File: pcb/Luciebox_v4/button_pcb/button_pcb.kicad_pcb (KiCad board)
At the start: 2 copper layers, 144 x 157.6 mm, 67 parts, among them T1 terminal_8x1, T2 terminal_8x1

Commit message: V4 main pcb ready for layouting
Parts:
- removed D1, D2, D3, D4, D5, D6, D7, D8: D_Schottky, Luciebox:smd_throughhole_2_pins
- removed the H1 at (110.8, 86.4)
- removed H10, H12, H14, H15, H17, H9: MountingHole, Luciebox:MountingHole_4.3mm_M4
- removed the H7 at (17.5, -38.4)
- removed the H8 at (77.5, -38.4)
- removed R1: R_Small, Luciebox:SIP-10
- removed R10, R11, R12, R13, R14, R15, R16, R17, R18, R2, R3, R4, R5, R6, R7, R8, R9: R_Small, Luciebox:1206_0805
- removed R19, R20, R21, R22, R23, R24, R25, R26, R27, R28, R29, R30: 10K, Luciebox_components:1206_0805
- removed S9: selector_knob, Luciebox_components:Rotary_Switch
- added BT1: 4xAA_Battery_holder, Luciebox_components:BatteryHolder_4xAA, B.Cu at (70.3, 89.1)
- added T3: terminal_8x1, Luciebox_components:Terminal_8x1_100mil, F.Cu at (19.1, 33.0)
- added T4: terminal_2x1, Luciebox_components:Terminal_2x1_100mil, F.Cu at (72.0, 28.5)
- H1: renamed from H16; footprint Luciebox:MountingHole_4.3mm_M4 -> Luciebox_components:MountingHole_4.3mm_M4
- H2: renamed from H6; footprint Luciebox:MountingHole_4.3mm_M4 -> Luciebox_components:MountingHole_4.3mm_M4
- H3: renamed from H13; footprint Luciebox:MountingHole_4.3mm_M4 -> Luciebox_components:MountingHole_4.3mm_M4
- H4: renamed from H11; footprint Luciebox:MountingHole_4.3mm_M4 -> Luciebox_components:MountingHole_4.3mm_M4
- H5: footprint Luciebox:MountingHole_4.3mm_M4 -> Luciebox_components:MountingHole_4.3mm_M4
- H6: renamed from H3; footprint Luciebox:MountingHole_4.3mm_M4 -> Luciebox_components:MountingHole_4.3mm_M4
- H7: renamed from H2; footprint Luciebox:MountingHole_4.3mm_M4 -> Luciebox_components:MountingHole_4.3mm_M4
- H8: renamed from H4; footprint Luciebox:MountingHole_4.3mm_M4 -> Luciebox_components:MountingHole_4.3mm_M4
- S1, S2, S3, S4, S5, S6, S7, S8: footprint Luciebox:button_LAZ16-11 -> Luciebox_components:button_LAZ16-11_big_holes
- T1, T2: footprint Luciebox:Terminal_8x1_100mil -> Luciebox_components:Terminal_8x1_100mil
- connect_for_vcc_as_common_anode1: footprint Luciebox:1206_0805 -> Luciebox_components:1206_0805
- moved H3 113.5 mm to (72.0, 61.0)
- moved H6 90.3 mm to (58.0, 25.0)
- moved connect_for_vcc_as_common_anode1 87.3 mm to (74.5, 34.0), turned to 90 degrees
- moved H7 76.1 mm to (58.0, 86.5)
- moved H8 66.2 mm to (20.0, 86.5)
- moved H5 52.9 mm to (20.0, 25.0)
- moved H2 47.7 mm to (72.0, 6.00)
- moved H1 40.5 mm to (6.00, 6.00)
- moved H4 38.5 mm to (6.00, 61.0)
- moved T2 27.4 mm to (39.4, 33.0)
- moved T1 7.48 mm to (59.7, 33.0)
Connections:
- S1 pad 5: VCC -> Net-(S1-Pad5)
- S2 pad 5: VCC -> Net-(S2-Pad5)
- S3 pad 5: VCC -> Net-(S3-Pad5)
- S4 pad 5: Net-(D4-Pad2) -> Net-(T2-Pad4)
- S5 pad 5: Net-(D5-Pad2) -> Net-(S5-Pad5)
- S6 pad 5: Net-(D6-Pad2) -> Net-(T2-Pad6)
- S7 pad 5: Net-(D7-Pad2) -> Net-(T2-Pad7)
- S8 pad 5: Net-(D8-Pad2) -> Net-(S8-Pad5)
- T1 pad 3: /ANALOG_1 -> Net-(S1-Pad4)
- T1 pad 4: /ANALOG_2 -> Net-(T1-Pad4)
- T1 pad 6: Net-(S1-Pad4) -> unconnected-(T1-Pad6)
- T2 pad 1: Net-(D1-Pad1) -> Net-(S1-Pad5)
- T2 pad 2: Net-(D2-Pad1) -> Net-(S2-Pad5)
- T2 pad 3: Net-(D3-Pad1) -> Net-(S3-Pad5)
- T2 pad 4: Net-(D4-Pad1) -> Net-(T2-Pad4)
- T2 pad 5: Net-(D5-Pad1) -> Net-(S5-Pad5)
- T2 pad 6: Net-(D6-Pad1) -> Net-(T2-Pad6)
- T2 pad 7: Net-(D7-Pad1) -> Net-(T2-Pad7)
- T2 pad 8: Net-(D8-Pad1) -> Net-(S8-Pad5)
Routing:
- net VCC: track 0.00 -> 244.7 mm, vias 0 -> 9
- net GND: track 0.00 -> 197.4 mm, vias 0 -> 1
- net Net-(S1-Pad4): track 0.00 -> 191.4 mm
- net Net-(S3-Pad3): track 0.00 -> 146.4 mm
- net Net-(S1-Pad5): track 0.00 -> 131.8 mm
- net Net-(T2-Pad4): track 0.00 -> 126.6 mm
- net Net-(S4-Pad3): track 0.00 -> 119.2 mm, vias 0 -> 5
- net Net-(S3-Pad5): track 0.00 -> 116.4 mm
- net Net-(S2-Pad5): track 0.00 -> 115.1 mm
- net Net-(S8-Pad3): track 0.00 -> 76.2 mm
- net Net-(S2-Pad3): track 0.00 -> 68.9 mm
- net Net-(S1-Pad3): track 0.00 -> 53.3 mm
- net Net-(S8-Pad5): track 0.00 -> 47.5 mm
- net Net-(S5-Pad5): track 0.00 -> 47.0 mm
- net Net-(S7-Pad3): track 0.00 -> 39.0 mm
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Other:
- board size 144 x 157.6 mm -> 78 x 100 mm
- board text added: "BAT+"
- board text added: "BAT-"
- board text added: "buttonsboard v2.0 2022-05 a luciebox extension by nonkel lode putting extra pret in the bak kicad project: button_pcb_4x_laz16-11"
- board text removed: "M2 M2.5 M3 M4"
- board text removed: "M5"
- board text removed: "M6"
- board text removed: "M8"
- board text removed: "buttonsboard v1.1 2020-12 a luciebox extension by nonkel lode putting extra pret in the bak kicad project: button_pcb_4x_laz16-11"

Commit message: layout main board start
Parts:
- added U1: 8X8PADS, Luciebox_components:8X8PADS_100mil, F.Cu at (40.2, 15.0)
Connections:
- net Net-(S1-Pad4) renamed /common Anode
- S1 pad 1: VCC -> Net-(BT1-Pad1)
- S1 pad 2: GND -> Net-(S1-Pad2)
- T1 pad 5: Net-(T1-Pad5) -> Net-(BT1-Pad1)
- T1 pad 6: unconnected-(T1-Pad6) -> Net-(S1-Pad2)
- T1 pad 7: unconnected-(T1-Pad7) -> Net-(S1-Pad3)
- T3 pad 1: Net-(S1-Pad3) -> unconnected-(T3-Pad1)
- T4 pad 2: Net-(T1-Pad5) -> Net-(BT1-Pad1)
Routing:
- net Net-(T1-Pad5): track 12.9 -> 0.00 mm
- net Net-(BT1-Pad1): track 0.00 -> 12.9 mm

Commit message: Delete Arduino Uno footprint. Line up bottonboard and main pcb
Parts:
- moved H5 14.0 mm to (6.00, 25.4)
- moved H6 14.0 mm to (72.0, 25.4)
- moved T4 5.99 mm to (66.0, 27.9)
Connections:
- U1 pad 1: unconnected-(U1-Pad1) -> VCC
- U1 pad 10: unconnected-(U1-Pad10) -> Net-(U1-Pad10)
- U1 pad 11: unconnected-(U1-Pad11) -> Net-(U1-Pad11)
- U1 pad 12: unconnected-(U1-Pad12) -> Net-(U1-Pad11)
- U1 pad 13: unconnected-(U1-Pad13) -> Net-(U1-Pad14)
- U1 pad 14: unconnected-(U1-Pad14) -> Net-(U1-Pad14)
- U1 pad 15: unconnected-(U1-Pad15) -> Net-(U1-Pad14)
- U1 pad 16: unconnected-(U1-Pad16) -> Net-(U1-Pad14)
- U1 pad 17: unconnected-(U1-Pad17) -> Net-(U1-Pad17)
- U1 pad 18: unconnected-(U1-Pad18) -> Net-(U1-Pad17)
- U1 pad 19: unconnected-(U1-Pad19) -> Net-(U1-Pad19)
- U1 pad 2: unconnected-(U1-Pad2) -> VCC
- U1 pad 20: unconnected-(U1-Pad20) -> Net-(U1-Pad19)
- U1 pad 21: unconnected-(U1-Pad21) -> Net-(U1-Pad21)
- U1 pad 22: unconnected-(U1-Pad22) -> Net-(U1-Pad21)
- U1 pad 23: unconnected-(U1-Pad23) -> Net-(U1-Pad21)
- U1 pad 24: unconnected-(U1-Pad24) -> Net-(U1-Pad21)
- U1 pad 3: unconnected-(U1-Pad3) -> VCC
- U1 pad 30: unconnected-(U1-Pad30) -> Net-(U1-Pad30)
- U1 pad 31: unconnected-(U1-Pad31) -> Net-(U1-Pad30)
- U1 pad 32: unconnected-(U1-Pad32) -> Net-(U1-Pad30)
- U1 pad 38: unconnected-(U1-Pad38) -> Net-(U1-Pad38)
- U1 pad 39: unconnected-(U1-Pad39) -> Net-(U1-Pad38)
- U1 pad 4: unconnected-(U1-Pad4) -> VCC
- U1 pad 40: unconnected-(U1-Pad40) -> Net-(U1-Pad38)
- U1 pad 46: unconnected-(U1-Pad46) -> Net-(U1-Pad46)
- U1 pad 47: unconnected-(U1-Pad47) -> Net-(U1-Pad46)
- U1 pad 48: unconnected-(U1-Pad48) -> Net-(U1-Pad46)
- U1 pad 5: unconnected-(U1-Pad5) -> VCC
- U1 pad 54: unconnected-(U1-Pad54) -> Net-(U1-Pad54)
- U1 pad 55: unconnected-(U1-Pad55) -> Net-(U1-Pad54)
- U1 pad 56: unconnected-(U1-Pad56) -> Net-(U1-Pad54)
- U1 pad 57: unconnected-(U1-Pad57) -> GND
- U1 pad 58: unconnected-(U1-Pad58) -> GND
- U1 pad 59: unconnected-(U1-Pad59) -> GND
- U1 pad 6: unconnected-(U1-Pad6) -> VCC
- U1 pad 60: unconnected-(U1-Pad60) -> GND
- U1 pad 61: unconnected-(U1-Pad61) -> GND
- U1 pad 62: unconnected-(U1-Pad62) -> GND
- U1 pad 63: unconnected-(U1-Pad63) -> GND
- U1 pad 64: unconnected-(U1-Pad64) -> GND
- U1 pad 7: unconnected-(U1-Pad7) -> VCC
- U1 pad 8: unconnected-(U1-Pad8) -> VCC
- U1 pad 9: unconnected-(U1-Pad9) -> Net-(U1-Pad10)
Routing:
- net unconnected-(T3-Pad1): track 0.00 -> 53.3 mm
- net Net-(S1-Pad3): track 53.3 -> 0.00 mm
- net Net-(BT1-Pad1): track 12.9 -> 7.18 mm
- net Net-(BT1-Pad2): track 12.9 -> 7.18 mm

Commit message: Main board pcb prevent interference with buttons from button board
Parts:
- moved T4 4.07 mm to (65.0, 24.0)
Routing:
- net Net-(BT1-Pad2): track 7.18 -> 10.7 mm
- net Net-(BT1-Pad1): track 7.18 -> 10.7 mm
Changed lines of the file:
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@@
       (net 17 "Net-(S7-Pad5)") (pinfunction "LED_-") (pintype "input"))
   )
-  (footprint "Luciebox_components:Terminal_8x1_100mil" locked (layer "F.Cu")
+  (footprint "Luciebox_components:Terminal_8x1_100mil" (layer "F.Cu")
     (at 39.37 33.02)
     (property "Sheetfile" "button_pcb.kicad_sch")
@@
       (clearance 2))
   )
-  (footprint "Luciebox_components:Terminal_8x1_100mil" locked (layer "F.Cu")
+  (footprint "Luciebox_components:Terminal_8x1_100mil" (layer "F.Cu")
     (at 59.69 33.02)
     (property "Sheetfile" "button_pcb.kicad_sch")
@@
       (net 16 "Net-(S6-Pad5)") (pinfunction "LED_-") (pintype "input"))
   )
-  (footprint "Luciebox_components:Terminal_8x1_100mil" locked (layer "F.Cu")
+  (footprint "Luciebox_components:Terminal_8x1_100mil" (layer "F.Cu")
     (at 19.05 33.02)
     (property "Sheetfile" "button_pcb.kicad_sch")
@@
   )
   (footprint "Luciebox_components:Terminal_2x1_100mil" (layer "F.Cu")
-    (at 66.04 27.94)
+    (at 65 24)
     (property "Sheetfile" "button_pcb.kicad_sch")
     (property "Sheetname" "")
@@
   (segment (start 11 57) (end 18.5 57) (width 0.25) (layer "B.Cu") (net 6))
   (segment (start 12.5 36.5) (end 8 36.5) (width 0.25) (layer "B.Cu") (net 6))
-  (segment (start 66.04 27.94) (end 60.96 33.02) (width 0.25) (layer "B.Cu") (net 7))
+  (segment (start 65 28.98) (end 60.96 33.02) (width 0.25) (layer "B.Cu") (net 7))
+  (segment (start 65 24) (end 65 28.98) (width 0.25) (layer "B.Cu") (net 7))
   (segment (start 14 36) (end 16.705489 33.294511) (width 0.25) (layer "B.Cu") (net 8))
   (segment (start 17.334922 31.945489) (end 19.245489 31.945489) (width 0.25) (layer "B.Cu") (net 8))
@@
   (segment (start 39.376478 45.172486) (end 40.026957 45.822965) (width 0.25) (layer "B.Cu") (net 17))
   (segment (start 45.72 33.02) (end 39.651469 39.088531) (width 0.25) (layer "B.Cu") (net 17))
-  (segment (start 63.5 27.94) (end 58.42 33.02) (width 0.25) (layer "B.Cu") (net 18))
+  (segment (start 62.46 28.98) (end 58.42 33.02) (width 0.25) (layer "B.Cu") (net 18))
+  (segment (start 62.46 24) (end 62.46 28.98) (width 0.25) (layer "B.Cu") (net 18))
   (segment (start 30.48 33.02) (end 36.624511 39.164511) (width 0.25) (layer "B.Cu") (net 19))
   (segment (start 12.627612 54.10098) (end 14.872388 54.10098) (width 0.25) (layer "B.Cu") (net 19))
@@
   (segment (start 7.444109 56.399022) (end 4.627612 56.39902) (width 0.25) (layer "B.Cu") (net 23))
   (segment (start 0.476468 52.247876) (end 0.476468 40.387828) (width 0.25) (layer "B.Cu") (net 23))
-  (group "" locked (id d0e64b79-2150-4840-bbf6-44e70b72fc6c)
-    (members
-      8269e9fd-85b6-4956-b9ff-6bc28fa3d59b
-      9396dbf5-aa3c-4ba1-a9ae-1945fbb2026c
-      b8dbe2de-283b-405e-95ac-e8f8950e16ea
-    )
-  )
 )

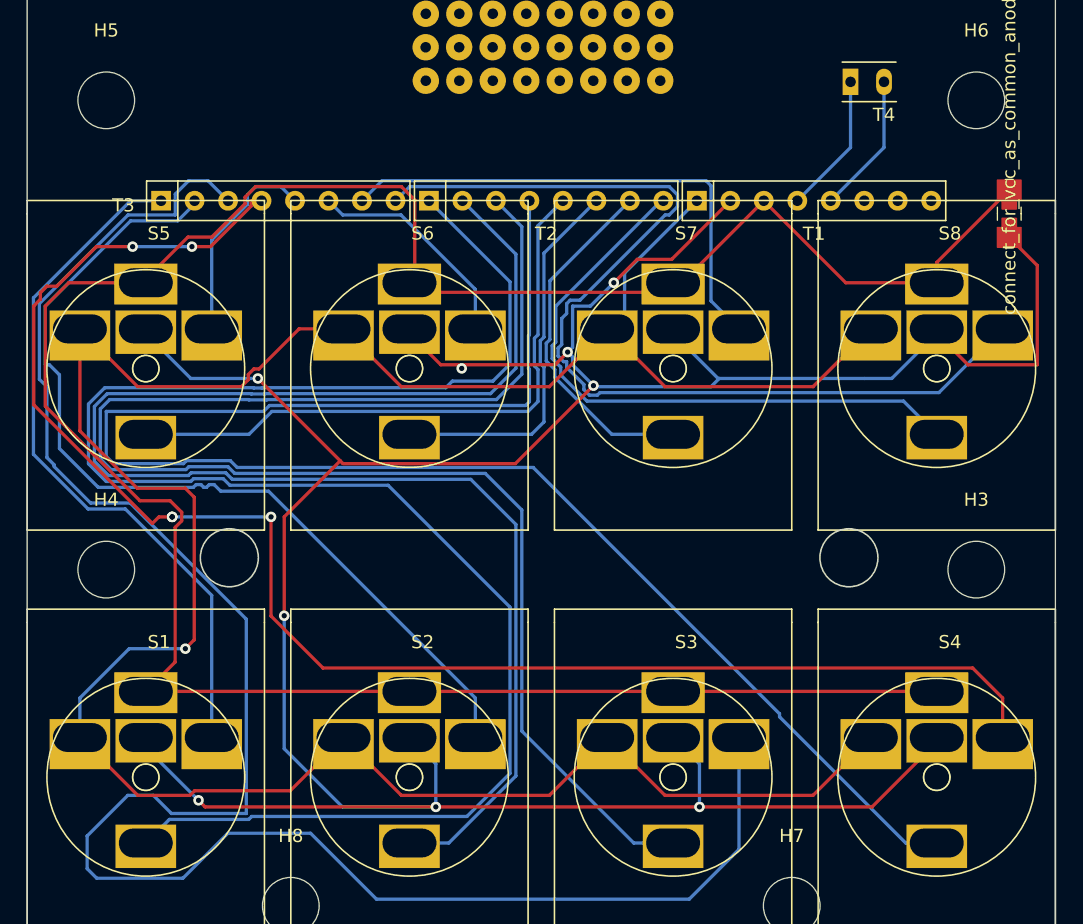
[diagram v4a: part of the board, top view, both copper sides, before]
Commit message: Moved boards connector. Main board ready for traces.
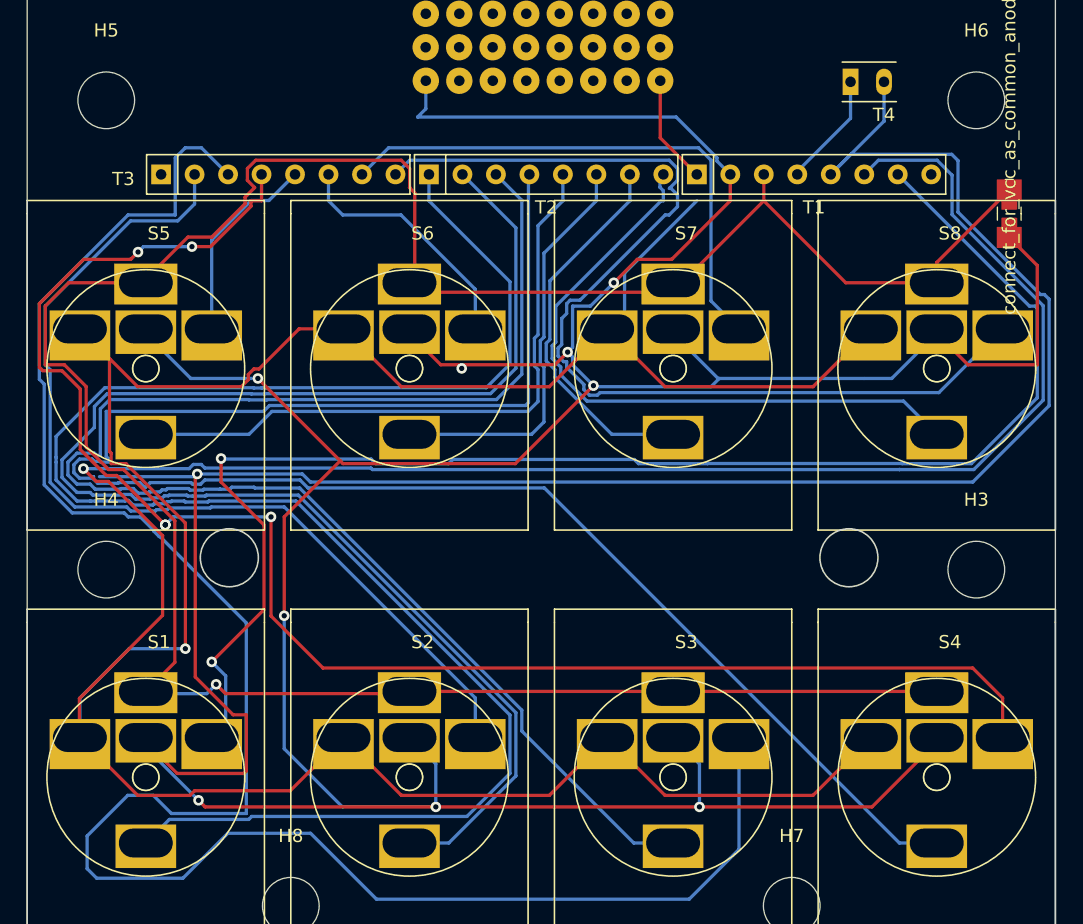
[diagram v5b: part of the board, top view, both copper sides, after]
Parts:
- moved T1 2.00 mm to (59.7, 31.0)
- moved T2 2.00 mm to (39.4, 31.0)
- moved T3 2.00 mm to (19.1, 31.0)
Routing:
- net Net-(BT1-Pad1): track 10.7 -> 149.4 mm, vias 0 -> 1
- net Net-(S1-Pad2): track 0.00 -> 127.6 mm, vias 0 -> 1
- net Net-(S1-Pad3): track 0.00 -> 111.0 mm, vias 0 -> 2
- net unconnected-(T3-Pad1): track 53.3 -> 0.00 mm
- net VCC: track 244.7 -> 275.4 mm
- net Net-(S4-Pad5): track 126.6 -> 135.3 mm
- net /common Anode: track 191.4 -> 198.3 mm, vias 0 -> 1
- net GND: track 197.4 -> 203.6 mm
- net Net-(S3-Pad3): track 146.4 -> 150.3 mm
- net Net-(S2-Pad3): track 68.9 -> 72.6 mm
- net Net-(S8-Pad3): track 76.2 -> 78.8 mm
- net Net-(S7-Pad3): track 39.0 -> 41.4 mm
- net Net-(S8-Pad5): track 47.5 -> 49.7 mm
- net Net-(S4-Pad3): track 119.2 -> 121.2 mm
- net Net-(S7-Pad5): track 27.1 -> 29.1 mm
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
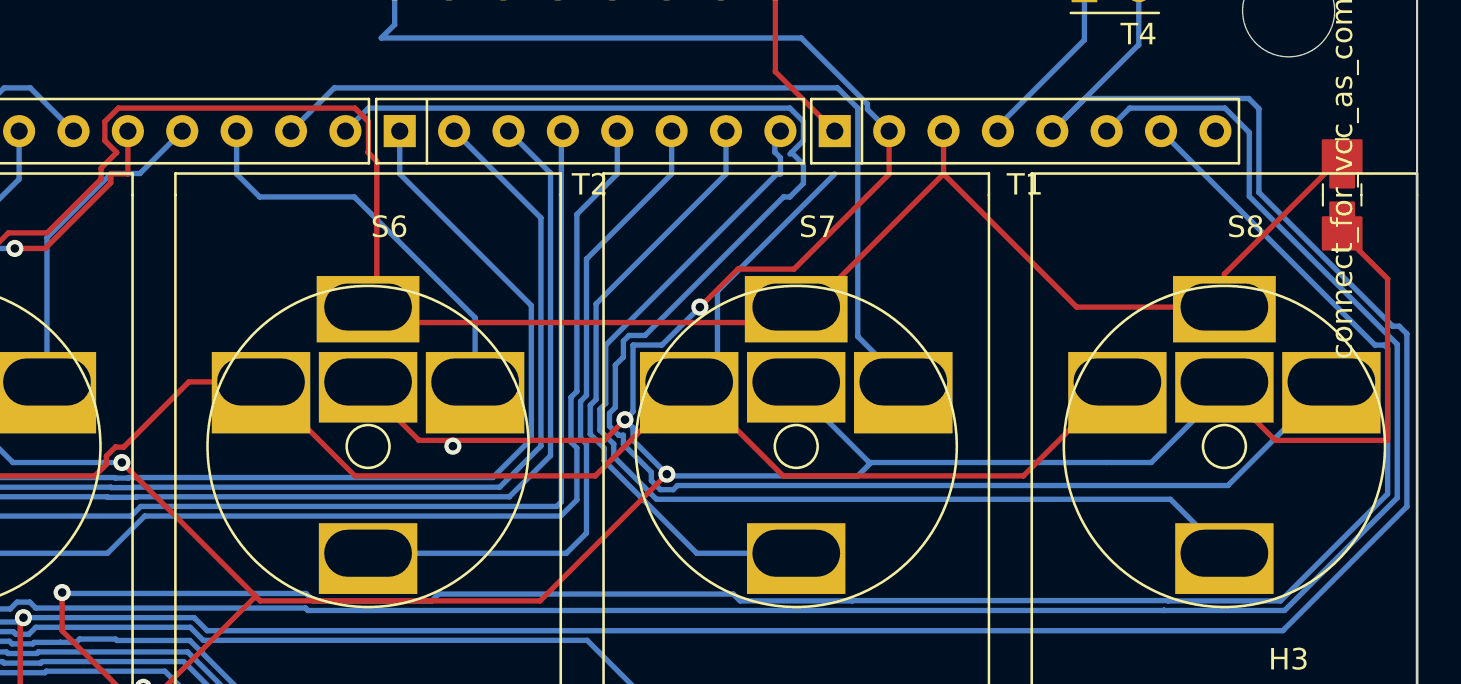
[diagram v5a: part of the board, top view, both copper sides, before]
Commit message: Add artwork. Copy screenshot to gimp to delete parts you don't want with silkscreen from original image. Than, generate new artwork. from burst, set to 150mm export
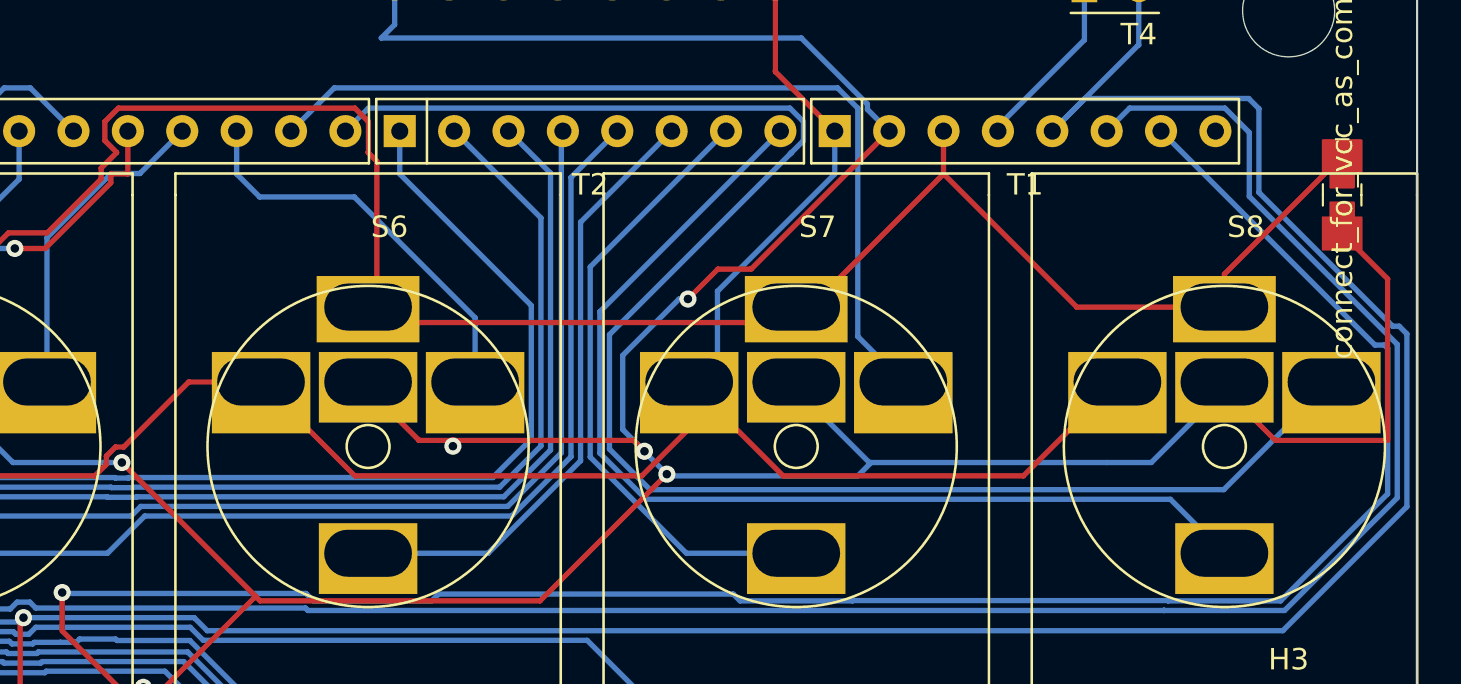
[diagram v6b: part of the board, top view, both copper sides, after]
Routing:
- net GND: track 203.6 -> 206.9 mm
- net Net-(S6-Pad5): track 31.2 -> 28.9 mm
- net Net-(S5-Pad5): track 49.0 -> 47.5 mm
- net Net-(S4-Pad5): track 135.3 -> 134.0 mm
- net Net-(S8-Pad3): track 78.8 -> 77.8 mm
- net VCC: track 275.4 -> 274.8 mm
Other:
- board text added: "button board v2.0 2022-11 a Nonkel Lode luciebox extension putting extra pret in the bak buttons: laz16-11"
- board text removed: "buttonsboard v2.0 2022-05 a luciebox extension by nonkel lode putting extra pret in the bak kicad project: button_pcb_4x_laz16-11"
